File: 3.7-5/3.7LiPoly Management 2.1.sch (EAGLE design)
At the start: 34 parts, among them J1 DX4R005HJ5R2000, J2 S2B-PH-SM4-TB(LF)(SN), T1 MMUN2133LT1G, U1 TPS61090RSAR, U2 MCP73871T-2CCI/ML

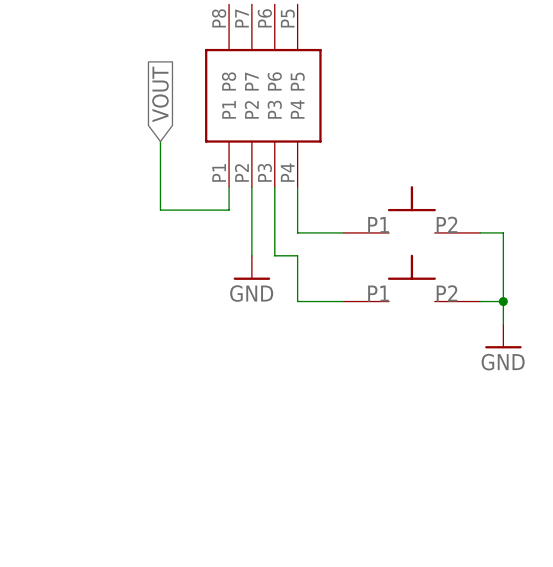
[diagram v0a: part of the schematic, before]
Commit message: Update
Moved shoulder buttons to LiPoly Management and extended LiPoly Management's dimensions. After looking at the boards in Fusion 360, I decided it would be better to have the shoulder buttons lower, rather than up high on RPi Zero Breakout. Rereouted LiPoly due to this.
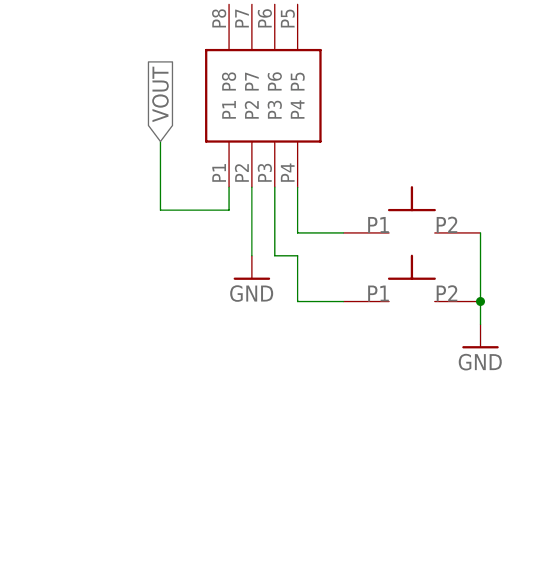
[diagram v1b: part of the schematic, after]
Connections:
- net N$10: now also U$3.P$1; no longer U$1.P$1
- net N$15: now also U$1.P$1; no longer U$3.P$1
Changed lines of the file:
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@@
 <instance part="LBO" gate="G$1" x="215.9" y="17.78" smashed="yes" rot="R270"/>
 <instance part="POWERON" gate="G$1" x="165.1" y="71.12" smashed="yes"/>
-<instance part="U$1" gate="G$1" x="289.56" y="40.64" smashed="yes"/>
-<instance part="U$3" gate="G$1" x="289.56" y="33.02" smashed="yes"/>
-<instance part="GND20" gate="1" x="299.72" y="27.94" smashed="yes">
-<attribute name="VALUE" x="297.18" y="25.4" size="1.778" layer="96"/>
+<instance part="U$1" gate="G$1" x="289.56" y="33.02" smashed="yes"/>
+<instance part="U$3" gate="G$1" x="289.56" y="40.64" smashed="yes"/>
+<instance part="GND20" gate="1" x="297.18" y="27.94" smashed="yes">
+<attribute name="VALUE" x="294.64" y="25.4" size="1.778" layer="96"/>
 </instance>
 </instances>
@@
 </segment>
 <segment>
+<pinref part="U$1" gate="G$1" pin="P$2"/>
 <pinref part="U$3" gate="G$1" pin="P$2"/>
+<wire x1="297.18" y1="33.02" x2="297.18" y2="40.64" width="0.1524" layer="91"/>
+<wire x1="297.18" y1="33.02" x2="297.18" y2="30.48" width="0.1524" layer="91"/>
+<junction x="297.18" y="33.02"/>
 <pinref part="GND20" gate="1" pin="GND"/>
-<wire x1="297.18" y1="33.02" x2="299.72" y2="33.02" width="0.1524" layer="91"/>
-<wire x1="299.72" y1="33.02" x2="299.72" y2="30.48" width="0.1524" layer="91"/>
-<pinref part="U$1" gate="G$1" pin="P$2"/>
-<wire x1="297.18" y1="40.64" x2="299.72" y2="40.64" width="0.1524" layer="91"/>
-<wire x1="299.72" y1="40.64" x2="299.72" y2="33.02" width="0.1524" layer="91"/>
-<junction x="299.72" y="33.02"/>
 </segment>
 </net>
@@
 <net name="N$10" class="0">
 <segment>
-<pinref part="U$1" gate="G$1" pin="P$1"/>
+<pinref part="U$3" gate="G$1" pin="P$1"/>
 <pinref part="H1" gate="A" pin="P4"/>
 <wire x1="281.94" y1="40.64" x2="276.86" y2="40.64" width="0.1524" layer="91"/>
@@
 <net name="N$15" class="0">
 <segment>
-<pinref part="U$3" gate="G$1" pin="P$1"/>
-<wire x1="281.94" y1="33.02" x2="276.86" y2="33.02" width="0.1524" layer="91"/>
-<wire x1="276.86" y1="33.02" x2="276.86" y2="38.1" width="0.1524" layer="91"/>
 <pinref part="H1" gate="A" pin="P3"/>
-<wire x1="276.86" y1="38.1" x2="274.32" y2="38.1" width="0.1524" layer="91"/>
-<wire x1="274.32" y1="38.1" x2="274.32" y2="45.72" width="0.1524" layer="91"/>
-</segment>
-</net>
+<wire x1="274.32" y1="45.72" x2="274.32" y2="38.1" width="0.1524" layer="91"/>
+<wire x1="274.32" y1="38.1" x2="276.86" y2="38.1" width="0.1524" layer="91"/>
+<pinref part="U$1" gate="G$1" pin="P$1"/>
+<wire x1="276.86" y1="38.1" x2="276.86" y2="33.02" width="0.1524" layer="91"/>
+<wire x1="276.86" y1="33.02" x2="281.94" y2="33.02" width="0.1524" layer="91"/>
+</segment>
+</net>
